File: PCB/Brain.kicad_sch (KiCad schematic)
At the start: 0 parts

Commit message: [Schem] Added sensors connectors & finished Step down circuit
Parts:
- added J14: Raspberry_Pi_Zero, symbol Connector:Raspberry_Pi_4
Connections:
- new net: J14.1 (3V3), J14.17 (3V3)
- new net: J14.14 (GND), J14.20 (GND), J14.25 (GND), J14.30 (GND), J14.34 (GND), J14.39 (GND), J14.6 (GND), J14.9 (GND)
- new net: J14.2 (5V), J14.4 (5V)
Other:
- added sheet ESP32-S3 (ESP32-S3.kicad_sch)
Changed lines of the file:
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@@
 	(generator_version "10.0")
 	(paper "A4")
+	(symbol
+		(lib_id "Connector:Raspberry_Pi_4")
+		(at 224.79 95.25 0)
+		(unit 1)
+		(body_style 1)
+		(exclude_from_sim no)
+		(in_bom yes)
+		(on_board yes)
+		(in_pos_files yes)
+		(dnp no)
+		(fields_autoplaced yes)
+		(property "Reference" "J14"
+			(at 224.79 64.77 0)
+			(show_name no)
+			(do_not_autoplace no)
+			(effects
+				(font
+					(size 1.27 1.27)
+				)
+			)
+		)
+		(property "Value" "Raspberry_Pi_Zero"
+			(at 224.79 67.31 0)
+			(show_name no)
+			(do_not_autoplace no)
+			(effects
+				(font
+					(size 1.27 1.27)
+				)
+			)
+		)
+		(property "Footprint" ""
+			(at 294.894 142.748 0)
+			(hide yes)
+			(show_name no)
+			(do_not_autoplace no)
+			(effects
+				(font
+					(size 1.27 1.27)
+				)
+				(justify left)
+			)
+		)
+		(property "Datasheet" "https://datasheets.raspberrypi.com/rpi4/raspberry-pi-4-datasheet.pdf"
+			(at 240.538 127.508 0)
+			(hide yes)
+			(show_name no)
+			(do_not_autoplace no)
+			(effects
+				(font
+					(size 1.27 1.27)
+				)
+				(justify left)
+			)
+		)
+		(property "Description" "Raspberry Pi 4 Model B"
+			(at 240.538 124.968 0)
+			(hide yes)
+			(show_name no)
+			(do_not_autoplace no)
+			(effects
+				(font
+					(size 1.27 1.27)
+				)
+				(justify left)
+			)
+		)
+		(pin "22"
+		)
+		(pin "9"
+		)
+		(pin "12"
+		)
+		(pin "8"
+		)
+		(pin "10"
+		)
+		(pin "14"
+		)
+		(pin "29"
+		)
+		(pin "31"
+		)
+		(pin "7"
+		)
+		(pin "15"
+		)
+		(pin "16"
+		)
+		(pin "3"
+		)
+		(pin "1"
+		)
+		(pin "13"
+		)
+		(pin "17"
+		)
+		(pin "2"
+		)
+		(pin "11"
+		)
+		(pin "19"
+		)
+		(pin "21"
+		)
+		(pin "6"
+		)
+		(pin "4"
+		)
+		(pin "5"
+		)
+		(pin "18"
+		)
+		(pin "20"
+		)
+		(pin "24"
+		)
+		(pin "26"
+		)
+		(pin "27"
+		)
+		(pin "23"
+		)
+		(pin "28"
+		)
+		(pin "25"
+		)
+		(pin "30"
+		)
+		(pin "33"
+		)
+		(pin "35"
+		)
+		(pin "36"
+		)
+		(pin "39"
+		)
+		(pin "38"
+		)
+		(pin "32"
+		)
+		(pin "34"
+		)
+		(pin "40"
+		)
+		(pin "37"
+		)
+		(instances
+			(project "PCB"
+				(path "/ce714510-8789-438c-9780-97c7c26e78af/0407dfcd-b798-4dd9-bff4-91ca1fe4759e"
+					(reference "J14")
+					(unit 1)
+				)
+			)
+		)
+	)
+	(sheet
+		(at 78.74 74.93)
+		(size 27.94 45.72)
+		(exclude_from_sim no)
+		(in_bom yes)
+		(on_board yes)
+		(dnp no)
+		(fields_autoplaced yes)
+		(stroke
+			(width 0.1524)
+			(type solid)
+		)
+		(fill
+			(color 0 0 0 0)
+		)
+		(property "Sheetname" "ESP32-S3"
+			(at 78.74 74.2184 0)
+			(show_name no)
+			(do_not_autoplace no)
+			(effects
+				(font
+					(size 1.27 1.27)
+				)
+				(justify left bottom)
+			)
+		)
+		(property "Sheetfile" "ESP32-S3.kicad_sch"
+			(at 78.74 121.2346 0)
+			(show_name no)
+			(do_not_autoplace no)
+			(effects
+				(font
+					(size 1.27 1.27)
+				)
+				(justify left top)
+			)
+		)
+		(instances
+			(project "PCB"
+				(path "/ce714510-8789-438c-9780-97c7c26e78af/0407dfcd-b798-4dd9-bff4-91ca1fe4759e"
+					(page "3")
+				)
+			)
+		)
+	)
 )

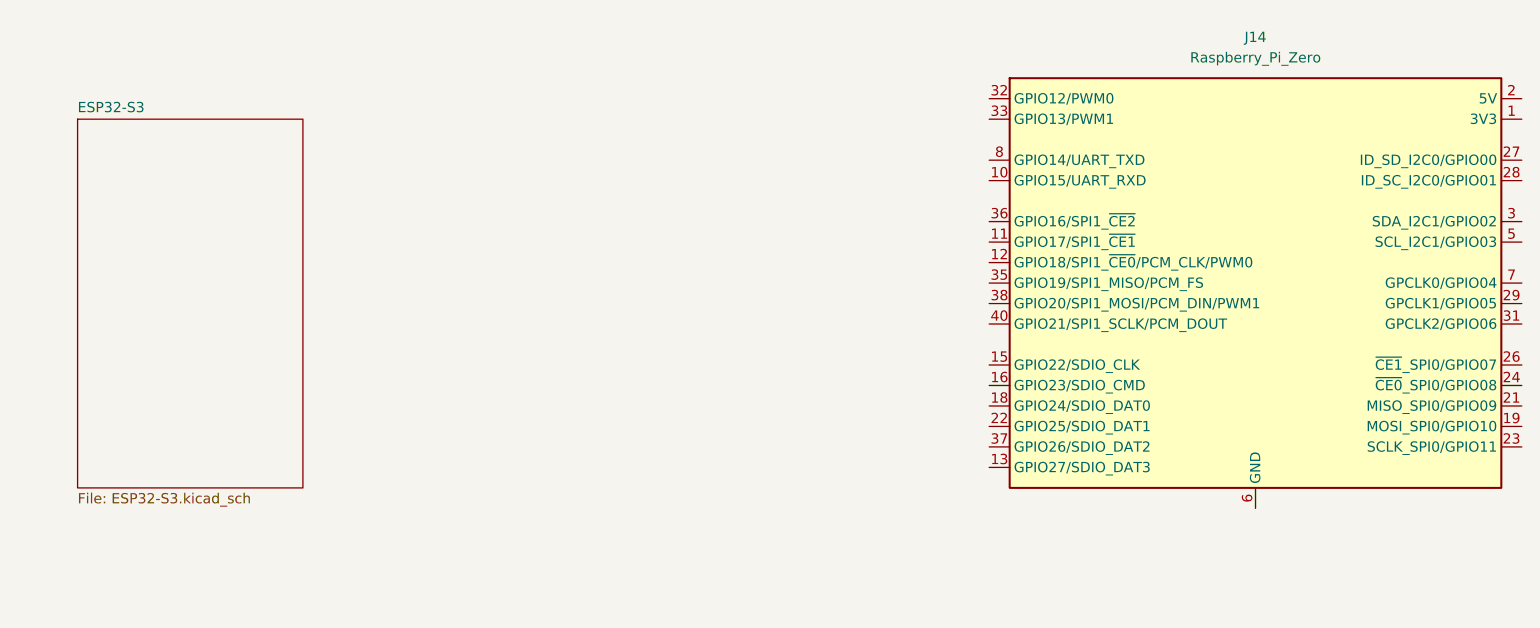
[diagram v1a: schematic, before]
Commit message: [Schem] Finished the Hierarchy Labels of all the pages
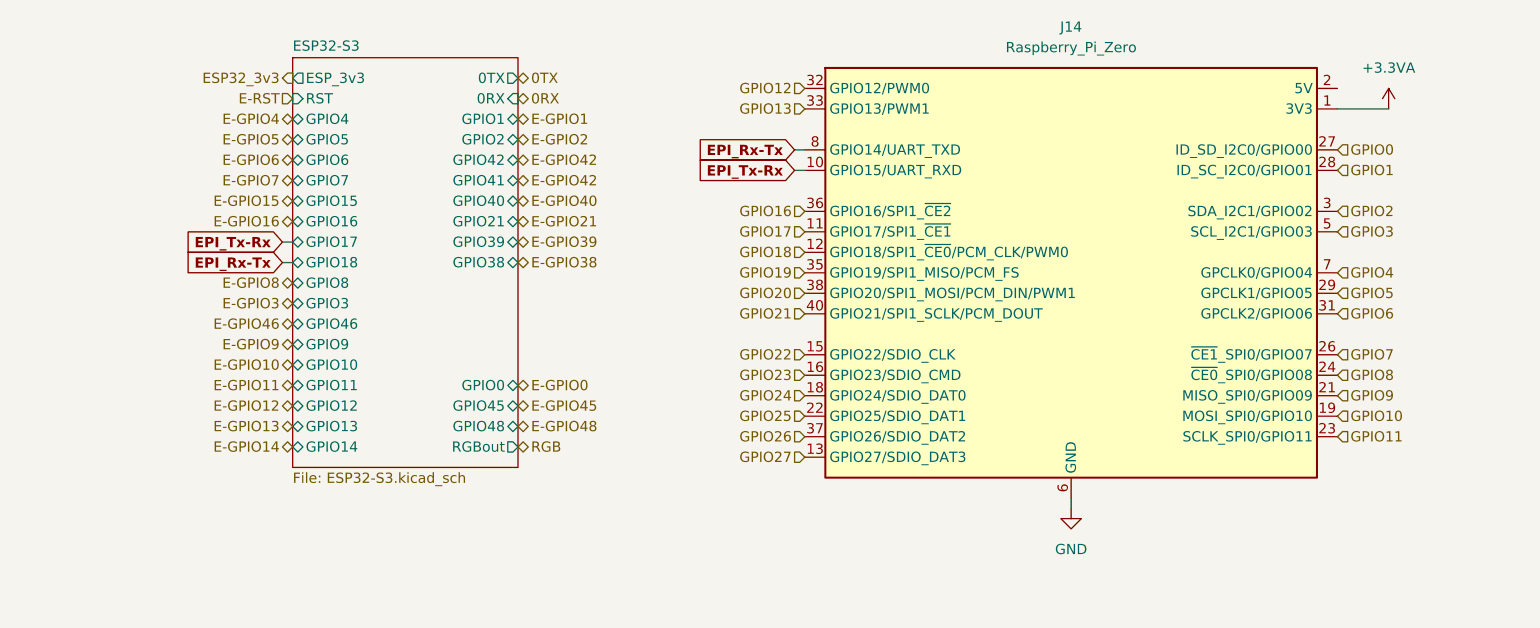
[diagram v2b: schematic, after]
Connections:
- net +3.3VA: now reaches J14.1 (3V3), J14.17 (3V3)
- net EPI_Tx-Rx: now reaches J14.10 (GPIO15/UART_RXD)
- net GPIO17: now reaches J14.11 (GPIO17/SPI1_~{CE1})
- net GPIO18: now reaches J14.12 (GPIO18/SPI1_~{CE0}/PCM_CLK/PWM0)
- net GPIO27: now reaches J14.13 (GPIO27/SDIO_DAT3)
- net GND: now reaches J14.14 (GND), J14.20 (GND), J14.25 (GND), J14.30 (GND), J14.34 (GND), J14.39 (GND), J14.6 (GND), J14.9 (GND)
- net GPIO22: now reaches J14.15 (GPIO22/SDIO_CLK)
- net GPIO23: now reaches J14.16 (GPIO23/SDIO_CMD)
- net GPIO24: now reaches J14.18 (GPIO24/SDIO_DAT0)
- net GPIO10: now reaches J14.19 (MOSI_SPI0/GPIO10)
- net GPIO9: now reaches J14.21 (MISO_SPI0/GPIO09)
- net GPIO25: now reaches J14.22 (GPIO25/SDIO_DAT1)
- net GPIO11: now reaches J14.23 (SCLK_SPI0/GPIO11)
- net GPIO8: now reaches J14.24 (~{CE0}_SPI0/GPIO08)
- net GPIO7: now reaches J14.26 (~{CE1}_SPI0/GPIO07)
- net GPIO0: now reaches J14.27 (ID_SD_I2C0/GPIO00)
- net GPIO1: now reaches J14.28 (ID_SC_I2C0/GPIO01)
- net GPIO5: now reaches J14.29 (GPCLK1/GPIO05)
- net GPIO2: now reaches J14.3 (SDA_I2C1/GPIO02)
- net GPIO6: now reaches J14.31 (GPCLK2/GPIO06)
- net GPIO12: now reaches J14.32 (GPIO12/PWM0)
- net GPIO13: now reaches J14.33 (GPIO13/PWM1)
- net GPIO19: now reaches J14.35 (GPIO19/SPI1_MISO/PCM_FS)
- net GPIO16: now reaches J14.36 (GPIO16/SPI1_~{CE2})
- net GPIO26: now reaches J14.37 (GPIO26/SDIO_DAT2)
- net GPIO20: now reaches J14.38 (GPIO20/SPI1_MOSI/PCM_DIN/PWM1)
- net GPIO21: now reaches J14.40 (GPIO21/SPI1_SCLK/PCM_DOUT)
- net GPIO3: now reaches J14.5 (SCL_I2C1/GPIO03)
- net GPIO4: now reaches J14.7 (GPCLK0/GPIO04)
- net EPI_Rx-Tx: now reaches J14.8 (GPIO14/UART_TXD)
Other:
- sheet ESP32-S3 ports: added 0RX, 0TX, ESP_3v3, GPIO0, GPIO1, GPIO10, GPIO11, GPIO12, GPIO13, GPIO14, GPIO15, GPIO16, GPIO17, GPIO18, GPIO2, GPIO21, GPIO3, GPIO38, GPIO39, GPIO4, GPIO40, GPIO41, GPIO42, GPIO45, GPIO46, GPIO48, GPIO5, GPIO6, GPIO7, GPIO8, GPIO9, RGBout, RST; removed none
- moved on the sheet: J14

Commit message: [Schem] Added all the net labels and connected the Dashboard screen
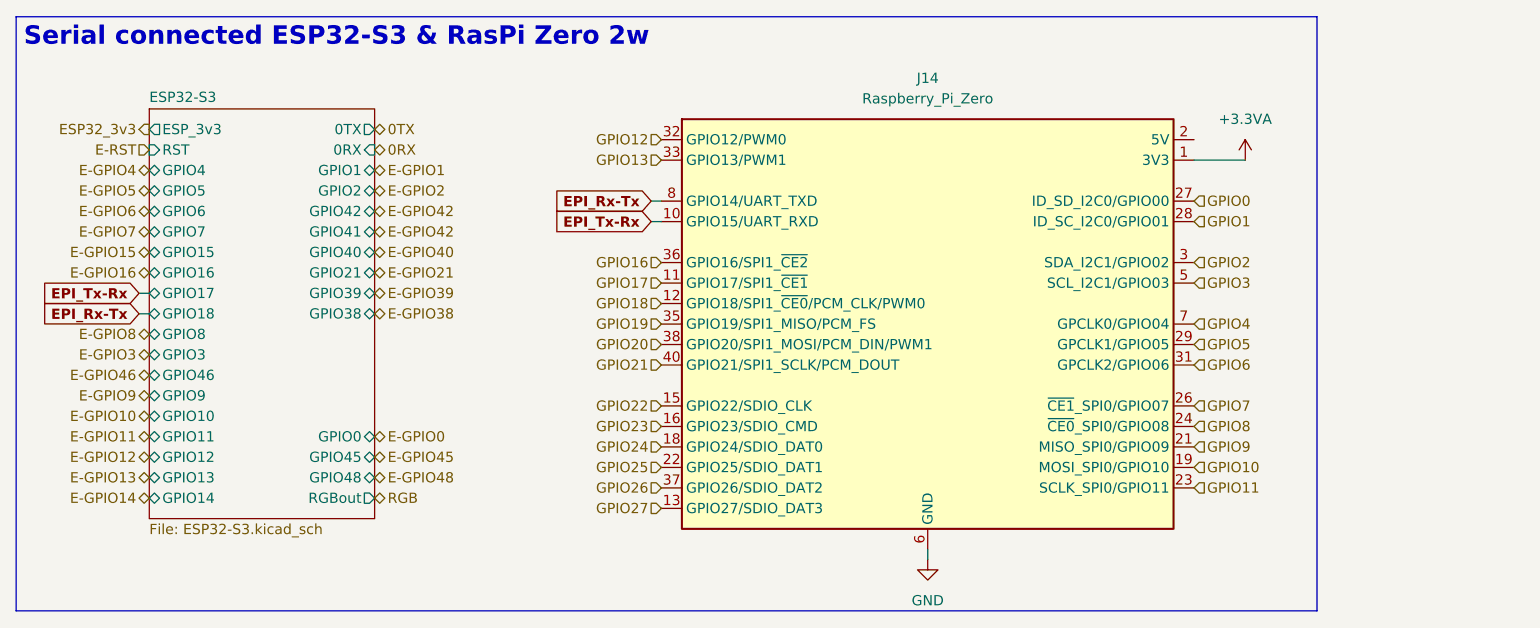
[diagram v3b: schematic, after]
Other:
- moved on the sheet: J14

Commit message: [PCB] Assigned all the footprints
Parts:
- J14: footprint (none) -> Connector_PinHeader_2.54mm:PinHeader_2x20_P2.54mm_Vertical
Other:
- sheet ESP32-S3 ports: added none; removed 0RX, 0TX
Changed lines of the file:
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@@
-		)
-	)
-	(hierarchical_label "0TX"
-		(shape bidirectional)
-		(at 115.57 76.2 0)
-		(effects
-			(font
-				(size 1.27 1.27)
-			)
-			(justify left)
 		)
 	)
@@
 			)
 			(justify right)
-		)
-	)
-	(hierarchical_label "0RX"
-		(shape bidirectional)
-		(at 115.57 78.74 0)
-		(effects
-			(font
-				(size 1.27 1.27)
-			)
-			(justify left)
 		)
 	)
@@
 			)
 		)
-		(property "Footprint" ""
+		(property "Footprint" "Connector_PinHeader_2.54mm:PinHeader_2x20_P2.54mm_Vertical"
 			(at 254.254 147.828 0)
 			(hide yes)
@@
 			)
 		)
-		(pin "0RX" input
-			(at 115.57 78.74 0)
-			(effects
-				(font
-					(size 1.27 1.27)
-				)
-				(justify right)
-			)
-		)
 		(pin "GPIO0" bidirectional
 			(at 115.57 114.3 0)
@@
 			)
 		)
-		(pin "ESP_3v3" output
+		(pin "ESP_3v3" input
 			(at 87.63 76.2 180)
 			(effects
@@
 			(effects
 				(font
-					(size 1.27 1.27)
-				)
-				(justify right)
-			)
-		)
-		(pin "0TX" output
-			(at 115.57 76.2 0)
-			(effects
-				(font

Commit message: [PCB] Traced the ESP's Type C
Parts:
- J14: footprint Connector_PinHeader_2.54mm:PinHeader_2x20_P2.54mm_Vertical -> Wall_E_FPs:MODULE_RASPBERRY_PI_ZERO_2_W
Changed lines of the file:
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@@
 			)
 		)
-		(property "Footprint" "Connector_PinHeader_2.54mm:PinHeader_2x20_P2.54mm_Vertical"
+		(property "Footprint" "Wall_E_FPs:MODULE_RASPBERRY_PI_ZERO_2_W"
 			(at 254.254 147.828 0)
 			(hide yes)

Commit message: [PCB] 95% finished the PCB
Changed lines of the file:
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@@
 		)
 	)
-	(hierarchical_label "E-GPIO42"
+	(hierarchical_label "E-GPIO41"
 		(shape bidirectional)
 		(at 115.57 88.9 0)
